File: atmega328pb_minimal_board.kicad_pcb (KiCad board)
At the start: 2 copper layers, 50.8 x 48.3 mm, 11 parts, among them J1 Power Connector, J2 Conn_02x05_Odd_Even, J3 Conn_01x02_Female, J4 Conn_01x04_Female, U1 ATmega328PB-AU, Y1 16MHz

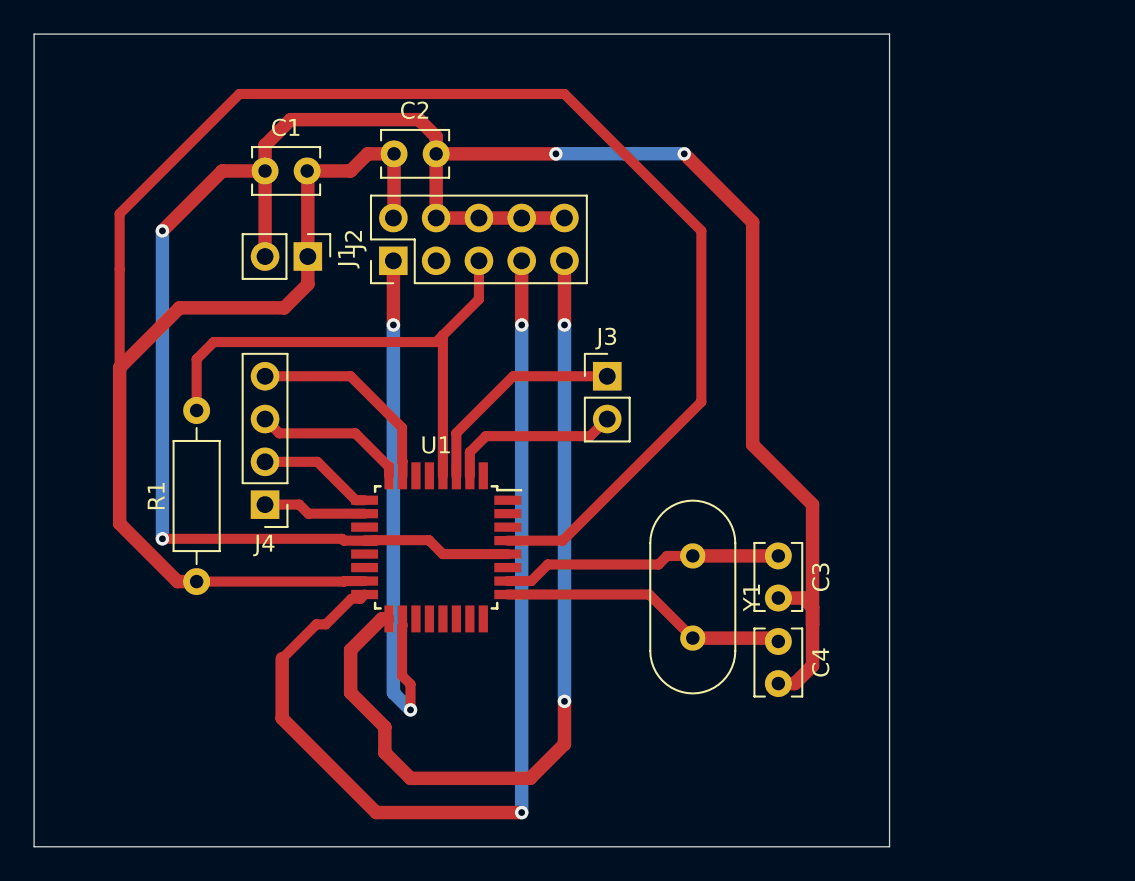
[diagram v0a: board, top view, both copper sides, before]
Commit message: change board layout
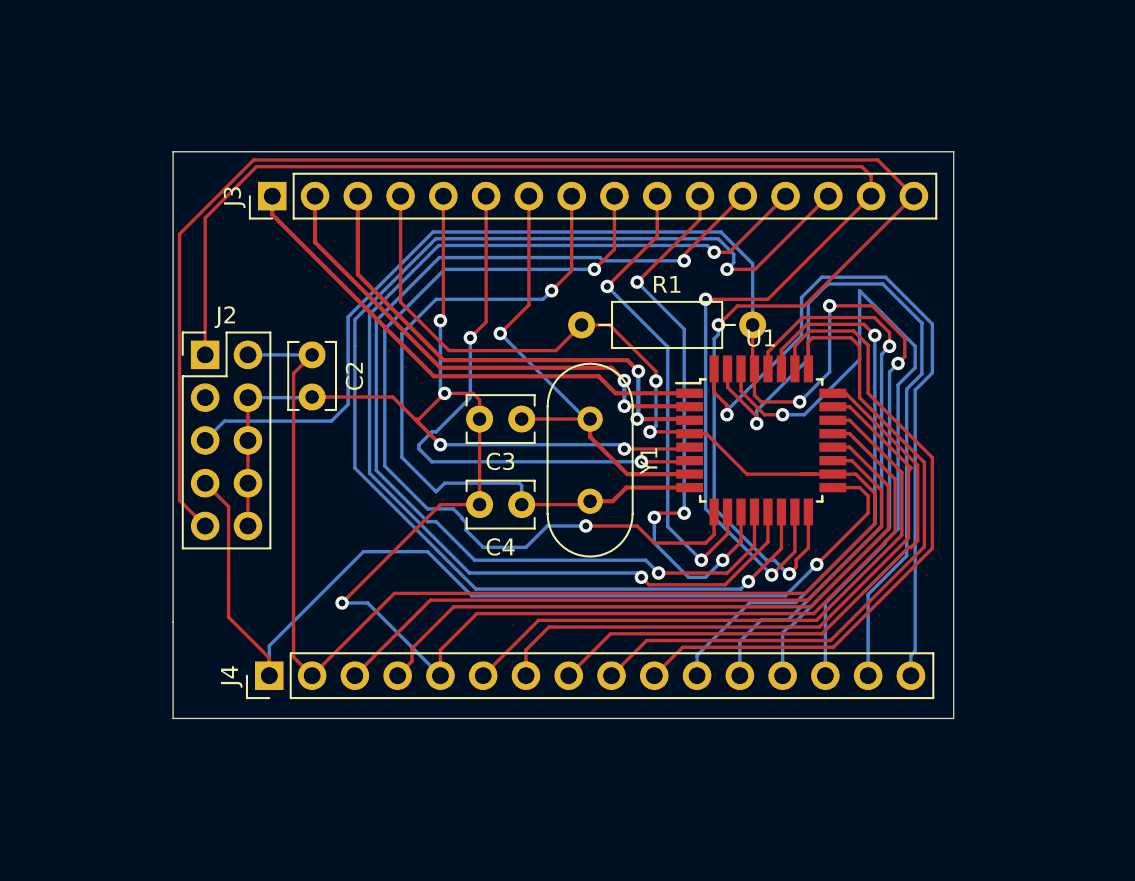
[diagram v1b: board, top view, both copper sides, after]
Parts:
- removed C1: 100nF, Capacitor_THT:C_Disc_D3.8mm_W2.6mm_P2.50mm
- removed J1: Power Connector, Connector_PinHeader_2.54mm:PinHeader_1x02_P2.54mm_Vertical
- J3: value Conn_01x02_Female -> Conn_01x16_Male; footprint Connector_PinHeader_2.54mm:PinHeader_1x02_P2.54mm_Vertical -> Connector_PinHeader_2.54mm:PinHeader_1x16_P2.54mm_Vertical
- J4: value Conn_01x04_Female -> Conn_01x16_Male; footprint Connector_PinHeader_2.54mm:PinHeader_1x04_P2.54mm_Vertical -> Connector_PinHeader_2.54mm:PinHeader_1x16_P2.54mm_Vertical
- moved R1 27.5 mm to (55.4, 35.1), turned to 0 degrees
- moved J3 22.6 mm to (37.0, 27.4), turned to 90 degrees
- moved U1 20.3 mm to (66.0, 41.9)
- moved C3 17.3 mm to (51.8, 40.6), turned to 180 degrees
- moved C4 17.3 mm to (51.8, 45.7), turned to 180 degrees
- moved C2 12.9 mm to (39.4, 36.8), turned to 270 degrees
- moved J2 12.5 mm to (33.0, 36.8), turned to 0 degrees
- moved J4 10.2 mm to (36.8, 55.9), turned to 90 degrees
- moved Y1 10.2 mm to (55.9, 40.6)
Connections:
- J3 pad 1: Net-(J3-Pad1) -> PIN1
- J3 pad 2: Net-(J3-Pad2) -> PIN2
- J4 pad 1: Net-(J4-Pad1) -> SCK
- J4 pad 2: Net-(J4-Pad2) -> VCC
- J4 pad 3: Net-(J4-Pad3) -> PIN19
- J4 pad 4: Net-(J4-Pad4) -> PIN20
- U1 pad 1: Net-(U1-Pad1) -> PIN1
- U1 pad 10: Net-(U1-Pad10) -> PIN10
- U1 pad 11: Net-(U1-Pad11) -> PIN11
- U1 pad 12: Net-(U1-Pad12) -> PIN12
- U1 pad 13: Net-(U1-Pad13) -> PIN13
- U1 pad 14: Net-(U1-Pad14) -> PIN14
- U1 pad 19: Net-(U1-Pad19) -> PIN19
- U1 pad 2: Net-(U1-Pad2) -> PIN2
- U1 pad 20: Net-(U1-Pad20) -> PIN20
- U1 pad 22: Net-(U1-Pad22) -> PIN22
- U1 pad 23: Net-(J4-Pad1) -> PIN23
- U1 pad 24: Net-(J4-Pad2) -> PIN24
- U1 pad 25: Net-(J4-Pad3) -> PIN25
- U1 pad 26: Net-(J4-Pad4) -> PIN26
- U1 pad 27: Net-(U1-Pad27) -> PIN27
- U1 pad 28: Net-(U1-Pad28) -> PIN28
- U1 pad 3: Net-(U1-Pad3) -> PIN3
- U1 pad 30: Net-(J3-Pad1) -> PIN30
- U1 pad 31: Net-(J3-Pad2) -> PIN31
- U1 pad 32: Net-(U1-Pad32) -> PIN32
- U1 pad 6: Net-(U1-Pad6) -> PIN6
- U1 pad 9: Net-(U1-Pad9) -> PIN9
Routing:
- net PIN14: track 0.00 -> 74.0 mm, vias 0 -> 2
- net PIN13: track 0.00 -> 66.6 mm, vias 0 -> 2
- net PIN12: track 0.00 -> 61.8 mm, vias 0 -> 2
- net RESET: track 31.9 -> 87.0 mm, vias 0 -> 3
- net MOSI: track 32.3 -> 85.0 mm
- net PIN9: track 0.00 -> 51.2 mm, vias 0 -> 2
- net MISO: track 50.8 -> 100.3 mm
- net PIN31: track 0.00 -> 42.8 mm, vias 0 -> 1
- net PIN32: track 0.00 -> 42.7 mm, vias 0 -> 1
- net PIN30: track 0.00 -> 40.8 mm, vias 0 -> 1
- net PIN19: track 0.00 -> 40.7 mm
- net PIN25: track 0.00 -> 40.2 mm
- net PIN20: track 0.00 -> 40.0 mm
- net PIN26: track 0.00 -> 39.7 mm
- net PIN22: track 0.00 -> 37.4 mm
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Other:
- board size 50.8 x 48.3 mm -> 46.4 x 33.7 mm

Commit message: add reset button, two usart headers and an LED
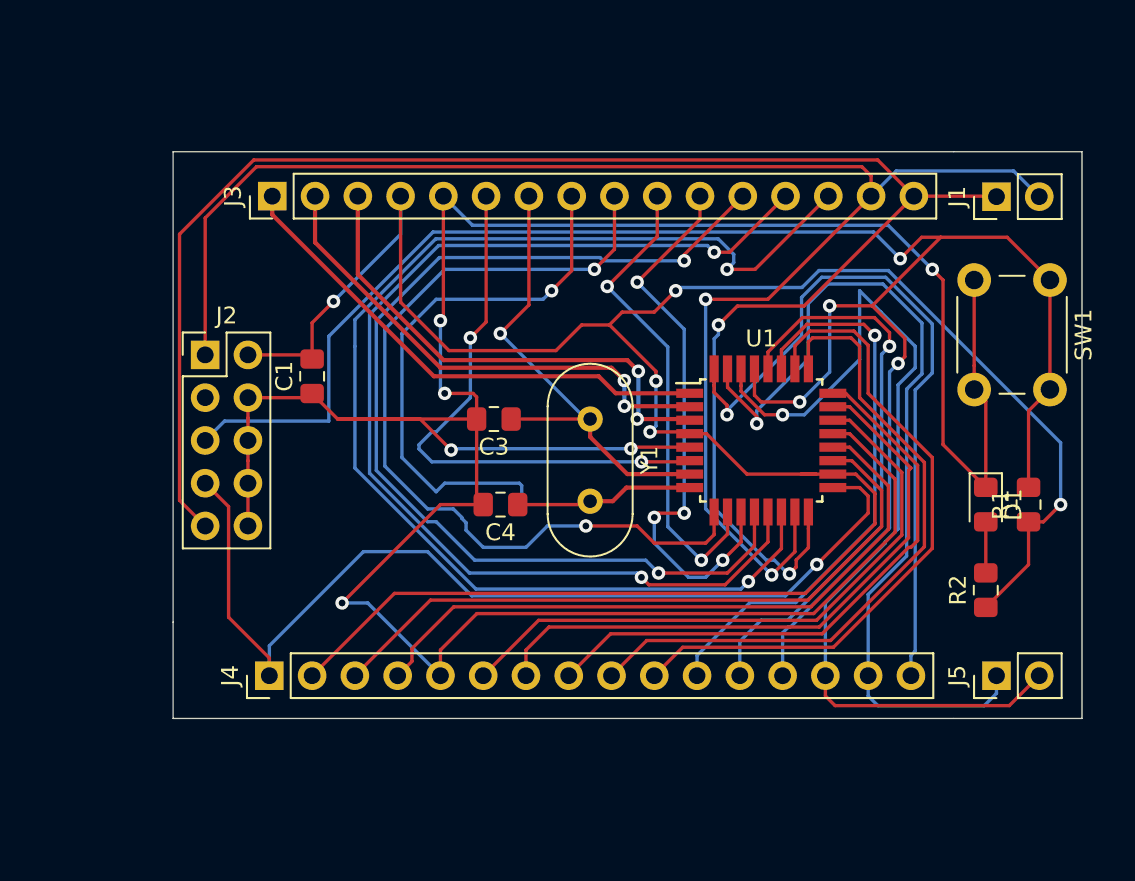
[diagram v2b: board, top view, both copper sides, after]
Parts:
- removed C2: 100nF, Capacitor_THT:C_Disc_D3.8mm_W2.6mm_P2.50mm
- added C1: 100nF, Capacitor_SMD:C_0805_2012Metric_Pad1.15x1.40mm_HandSolder, F.Cu at (39.4, 38.1)
- added D1: LED_Small, LED_SMD:LED_0805_2012Metric_Pad1.15x1.40mm_HandSolder, F.Cu at (79.4, 45.7)
- added J1: Conn_01x02_Male, Connector_PinHeader_2.54mm:PinHeader_1x02_P2.54mm_Vertical, F.Cu at (80.0, 27.4)
- added J5: Conn_01x02_Male, Connector_PinHeader_2.54mm:PinHeader_1x02_P2.54mm_Vertical, F.Cu at (80.0, 55.9)
- added R2: 100 Ohm, Resistor_SMD:R_0805_2012Metric_Pad1.15x1.40mm_HandSolder, F.Cu at (79.4, 50.8)
- added SW1: Reset, Button_Switch_THT:SW_PUSH_6mm_H5mm, F.Cu at (83.2, 32.4)
- C3, C4: footprint Capacitor_THT:C_Disc_D3.8mm_W2.6mm_P2.50mm -> Capacitor_SMD:C_0805_2012Metric_Pad1.15x1.40mm_HandSolder
- R1: footprint Resistor_THT:R_Axial_DIN0207_L6.3mm_D2.5mm_P10.16mm_Horizontal -> Resistor_SMD:R_0805_2012Metric_Pad1.15x1.40mm_HandSolder
- moved R1 28.6 mm to (81.9, 45.7), turned to 90 degrees
- moved C3 1.65 mm to (50.2, 40.6)
- moved C4 1.26 mm to (50.6, 45.7)
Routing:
- net GND: track 117.7 -> 179.6 mm, vias 6 -> 7
- net VCC: track 106.7 -> 143.2 mm, vias 2 -> 5
- net RESET: track 87.0 -> 118.3 mm, vias 3 -> 4
- net PIN30: track 40.8 -> 55.7 mm
- net MOSI: track 85.0 -> 96.3 mm
- net PIN31: track 42.8 -> 53.2 mm
- net MISO: track 100.3 -> 105.2 mm
- net Net-(D1-Pad2): track 0.00 -> 3.03 mm
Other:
- board size 46.4 x 33.7 mm -> 54 x 33.7 mm

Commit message: change 2 1x16 male pin headers to female connectors
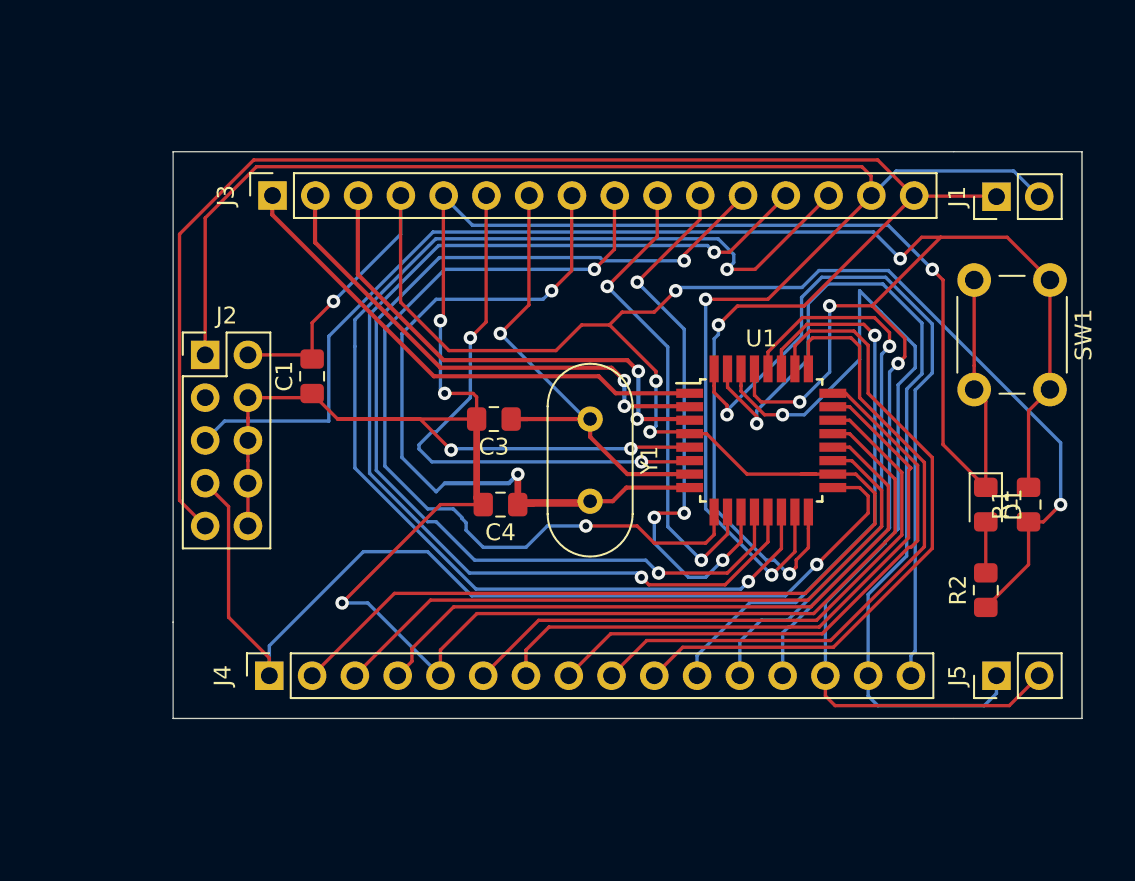
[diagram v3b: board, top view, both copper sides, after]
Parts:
- J3, J4: footprint Connector_PinHeader_2.54mm:PinHeader_1x16_P2.54mm_Vertical -> Connector_PinSocket_2.54mm:PinSocket_1x16_P2.54mm_Vertical
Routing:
- net XTAL2: track 43.4 -> 53.5 mm, vias 1 -> 2
- net XTAL1: track 28.2 -> 33.9 mm
- net GND: vias 7 -> 6

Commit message: add some pin labels
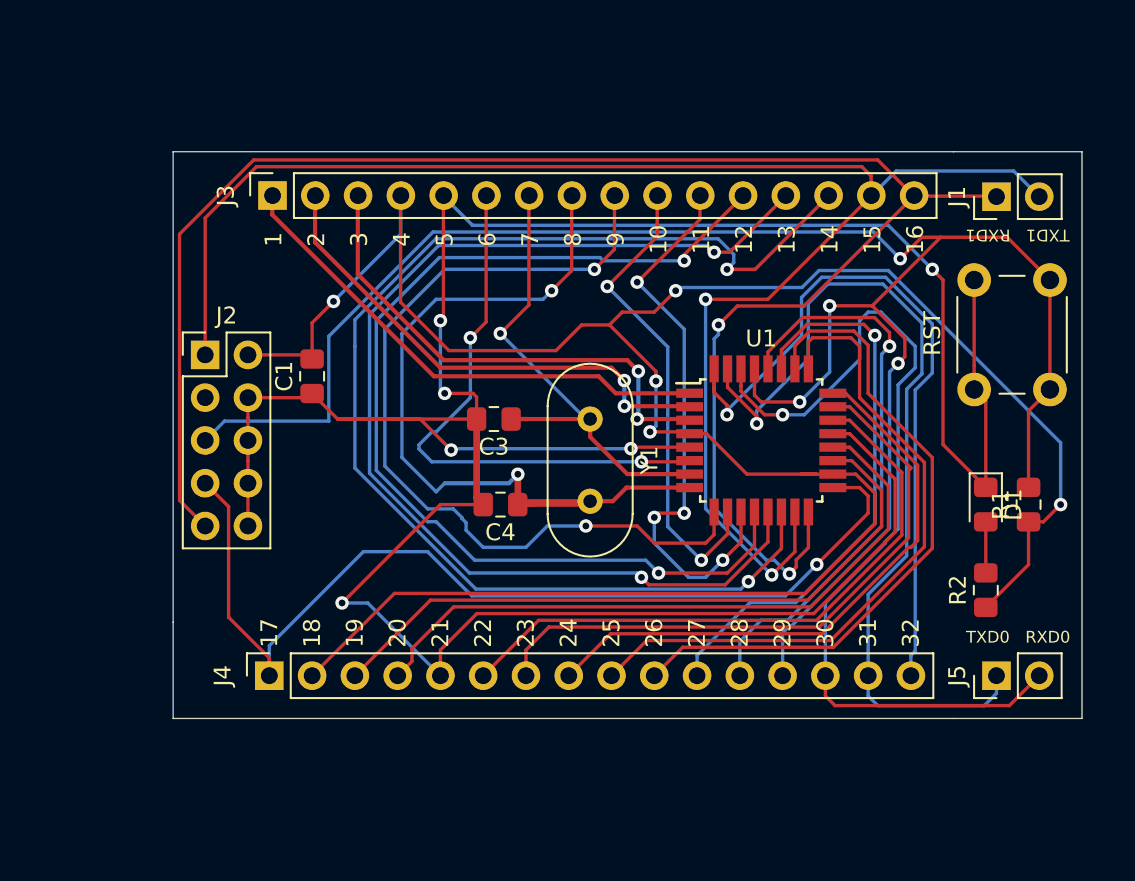
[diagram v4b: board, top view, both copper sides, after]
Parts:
- removed SW1: Reset, Button_Switch_THT:SW_PUSH_6mm_H5mm
- added RST: Reset, Button_Switch_THT:SW_PUSH_6mm_H5mm, F.Cu at (83.2, 32.4)
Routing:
- net PIN30: track 55.7 -> 53.6 mm
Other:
- board text added: "1"
- board text added: "10"
- board text added: "11"
- board text added: "12"
- board text added: "13"
- board text added: "14"
- board text added: "15"
- board text added: "16"
- board text added: "17"
- board text added: "18"
- board text added: "19"
- board text added: "2"
- board text added: "20"
- board text added: "21"
- board text added: "22"
- board text added: "23"
- board text added: "24"
- board text added: "25"
- board text added: "26"
- board text added: "27"
- board text added: "28"
- board text added: "29"
- board text added: "3"
- board text added: "30"
- board text added: "31"
- board text added: "32"
- board text added: "4"
- board text added: "5"
- board text added: "6"
- board text added: "7"
- board text added: "8"
- board text added: "9"
- board text added: "RXD0"
- board text added: "RXD1"
- board text added: "TXD0"
- board text added: "TXD1"
- board text added: "Yovan Naumovski - 2019 Atmega328PB Miniboard v0.1"
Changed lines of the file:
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@@
   (general
     (thickness 1.6)
-    (drawings 7)
-    (tracks 496)
+    (drawings 44)
+    (tracks 497)
     (zones 0)
     (modules 14)
@@
   )
   (setup
-    (last_trace_width 0.4)
+    (last_trace_width 0.2)
     (user_trace_width 0.2)
     (user_trace_width 0.4)
@@
     (visible_elements FFFFFF7F)
     (pcbplotparams
-      (layerselection 0x00000_7fffffff)
+      (layerselection 0x010fc_ffffffff)
       (usegerberextensions false)
       (usegerberattributes false)
@@
       (padsonsilk false)
       (subtractmaskfromsilk false)
-      (outputformat 4)
+      (outputformat 1)
       (mirror false)
-      (drillshape 2)
+      (drillshape 0)
       (scaleselection 1)
-      (outputdirectory ""))
+      (outputdirectory "/home/yovan/Desktop/atmega_miniboard_1/"))
   )
   (net 0 "")
@@
     (descr "tactile push button, 6x6mm e.g. PHAP33xx series, height=5mm")
     (tags "tact sw push 6mm")
-    (fp_text reference SW1 (at 3.25 -2 90) (layer F.SilkS)
+    (fp_text reference RST (at 3.175 6.985 90) (layer F.SilkS)
       (effects (font (size 1 1) (thickness 0.15)))
     )
@@
       (rotate (xyz 0 0 0))
     )
+  )
+  (gr_text "Yovan Naumovski - 2019\nAtmega328PB Miniboard v0.1" (at 51.054 52.07) (layer B.SilkS)
+    (effects (font (size 0.7 0.7) (thickness 0.15)) (justify mirror))
+  )
+  (gr_text TXD1 (at 83.058 29.718 180) (layer F.SilkS)
+    (effects (font (size 0.7 0.7) (thickness 0.15)))
+  )
+  (gr_text RXD1 (at 79.502 29.718 180) (layer F.SilkS)
+    (effects (font (size 0.7 0.7) (thickness 0.15)))
+  )
+  (gr_text TXD0 (at 79.502 53.594) (layer F.SilkS)
+    (effects (font (size 0.7 0.7) (thickness 0.15)))
+  )
+  (gr_text RXD0 (at 83.058 53.594) (layer F.SilkS)
+    (effects (font (size 0.7 0.7) (thickness 0.15)))
+  )
+  (gr_text 32 (at 74.93 53.34 90) (layer F.SilkS)
+    (effects (font (size 1 1) (thickness 0.25)))
+  )
+  (gr_text 31 (at 72.39 53.34 90) (layer F.SilkS)
+    (effects (font (size 1 1) (thickness 0.25)))
+  )
+  (gr_text 30 (at 69.85 53.34 90) (layer F.SilkS)
+    (effects (font (size 1 1) (thickness 0.25)))
+  )
+  (gr_text 29 (at 67.31 53.34 90) (layer F.SilkS)
+    (effects (font (size 1 1) (thickness 0.25)))
+  )
+  (gr_text 28 (at 64.77 53.34 90) (layer F.SilkS)
+    (effects (font (size 1 1) (thickness 0.25)))
+  )
+  (gr_text 27 (at 62.23 53.34 90) (layer F.SilkS)
+    (effects (font (size 1 1) (thickness 0.25)))
+  )
+  (gr_text 26 (at 59.69 53.34 90) (layer F.SilkS)
+    (effects (font (size 1 1) (thickness 0.25)))
+  )
+  (gr_text 25 (at 57.15 53.34 90) (layer F.SilkS)
+    (effects (font (size 1 1) (thickness 0.25)))
+  )
+  (gr_text 24 (at 54.61 53.34 90) (layer F.SilkS)
+    (effects (font (size 1 1) (thickness 0.25)))
+  )
+  (gr_text 23 (at 52.07 53.34 90) (layer F.SilkS)
+    (effects (font (size 1 1) (thickness 0.25)))
+  )
+  (gr_text 22 (at 49.53 53.34 90) (layer F.SilkS)
+    (effects (font (size 1 1) (thickness 0.25)))
+  )
+  (gr_text 21 (at 46.99 53.34 90) (layer F.SilkS)
+    (effects (font (size 1 1) (thickness 0.25)))
+  )
+  (gr_text 20 (at 44.45 53.34 90) (layer F.SilkS)
+    (effects (font (size 1 1) (thickness 0.25)))
+  )
+  (gr_text 19 (at 41.91 53.34 90) (layer F.SilkS)
+    (effects (font (size 1 1) (thickness 0.25)))
+  )
+  (gr_text 18 (at 39.37 53.34 90) (layer F.SilkS)
+    (effects (font (size 1 1) (thickness 0.25)))
+  )
+  (gr_text 17 (at 36.83 53.34 90) (layer F.SilkS)
+    (effects (font (size 1 1) (thickness 0.25)))
+  )
+  (gr_text 16 (at 75.184 29.972 90) (layer F.SilkS)
+    (effects (font (size 1 1) (thickness 0.25)))
+  )
+  (gr_text 15 (at 72.644 29.972 90) (layer F.SilkS)
+    (effects (font (size 1 1) (thickness 0.25)))
+  )
+  (gr_text 14 (at 70.104 29.972 90) (layer F.SilkS)
+    (effects (font (size 1 1) (thickness 0.25)))
+  )
+  (gr_text 13 (at 67.564 29.972 90) (layer F.SilkS)
+    (effects (font (size 1 1) (thickness 0.25)))
+  )
+  (gr_text 12 (at 65.024 29.972 90) (layer F.SilkS)
+    (effects (font (size 1 1) (thickness 0.25)))
+  )
+  (gr_text 11 (at 62.484 29.972 90) (layer F.SilkS)
+    (effects (font (size 1 1) (thickness 0.25)))
+  )
+  (gr_text 10 (at 59.944 29.972 90) (layer F.SilkS)
+    (effects (font (size 1 1) (thickness 0.25)))
+  )
+  (gr_text 9 (at 57.404 29.972 90) (layer F.SilkS)
+    (effects (font (size 1 1) (thickness 0.25)))
+  )
+  (gr_text 8 (at 54.864 29.972 90) (layer F.SilkS)
+    (effects (font (size 1 1) (thickness 0.25)))
+  )
+  (gr_text 7 (at 52.324 29.972 90) (layer F.SilkS)
+    (effects (font (size 1 1) (thickness 0.25)))
+  )
+  (gr_text 6 (at 49.784 29.972 90) (layer F.SilkS)
+    (effects (font (size 1 1) (thickness 0.25)))
+  )
+  (gr_text 5 (at 47.244 29.972 90) (layer F.SilkS)
+    (effects (font (size 1 1) (thickness 0.25)))
+  )
+  (gr_text 4 (at 44.704 29.972 90) (layer F.SilkS)
+    (effects (font (size 1 1) (thickness 0.25)))
+  )
+  (gr_text 3 (at 42.164 29.972 90) (layer F.SilkS)
+    (effects (font (size 1 1) (thickness 0.25)))
+  )
+  (gr_text 2 (at 39.624 29.972 90) (layer F.SilkS)
+    (effects (font (size 1 1) (thickness 0.25)))
+  )
+  (gr_text 1 (at 37.084 29.972 90) (layer F.SilkS)
+    (effects (font (size 1 1) (thickness 0.25)))
   )
   (gr_line (start 85.09 58.42) (end 77.47 58.42) (layer Edge.Cuts) (width 0.05))
@@
   (segment (start 75.184 37.592) (end 75.184 36.322) (width 0.2) (layer B.Cu) (net 22))
   (segment (start 75.184 36.322) (end 73.152 34.29) (width 0.2) (layer B.Cu) (net 22))
-  (segment (start 73.152 34.29) (end 71.882 33.02) (width 0.2) (layer B.Cu) (net 22))
   (via (at 67.31 40.386) (size 0.8) (drill 0.4) (layers F.Cu B.Cu) (net 22))
   (segment (start 68.600002 40.386) (end 67.31 40.386) (width 0.2) (layer B.Cu) (net 22))
-  (segment (start 71.882 33.02) (end 71.882 37.104002) (width 0.2) (layer B.Cu) (net 22))
   (segment (start 71.882 37.104002) (end 68.600002 40.386) (width 0.2) (layer B.Cu) (net 22))
   (segment (start 64.84 38.66) (end 64.84 37.66) (width 0.2) (layer F.Cu) (net 22))
@@
   (segment (start 80.772 57.658) (end 82.55 55.88) (width 0.2) (layer F.Cu) (net 22))
   (segment (start 70.425919 57.658) (end 80.772 57.658) (width 0.2) (layer F.Cu) (net 22))
+  (segment (start 73.152 34.29) (end 72.39 34.29) (width 0.2) (layer B.Cu) (net 22))
+  (segment (start 72.39 34.29) (end 71.882 34.798) (width 0.2) (layer B.Cu) (net 22))
+  (segment (start 71.882 34.798) (end 71.882 37.084) (width 0.2) (layer B.Cu) (net 22))
   (segment (start 73.66 35.508349) (end 73.66 36.322) (width 0.2) (layer F.Cu) (net 23))
   (segment (start 72.765621 34.61397) (end 73.66 35.508349) (width 0.2) (layer F.Cu) (net 23))
